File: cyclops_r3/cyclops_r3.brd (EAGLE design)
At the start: 124.5 x 79.9 mm, 96 parts, among them Q1 BC817, Q2 IRF510, U1 MCP4921, U2 317-N, U3 TLV3701, U4 337-N, U5 ADR03, U6 OP1177, U7 LTC2052, U8 ZXTD45

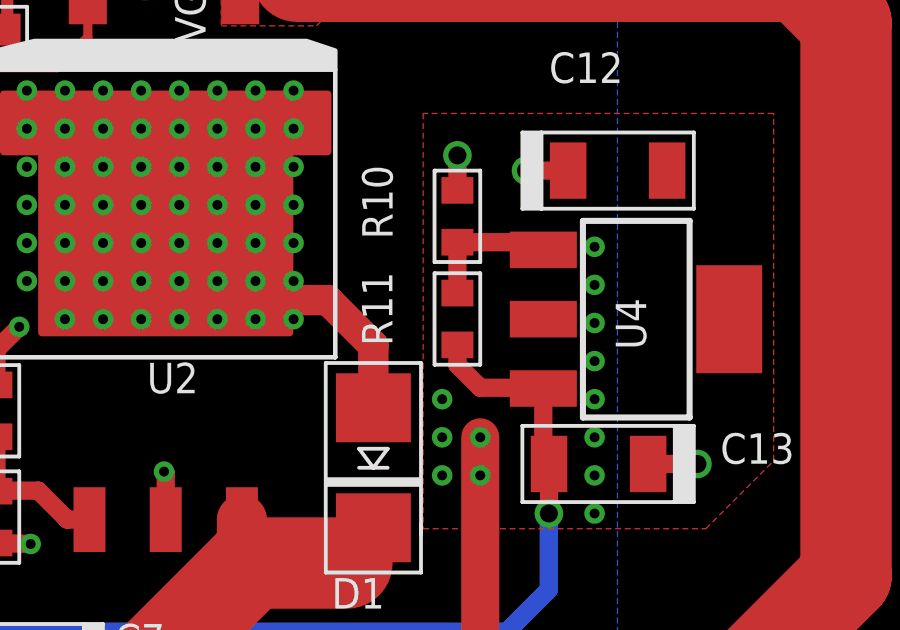
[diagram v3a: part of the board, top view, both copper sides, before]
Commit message: Added some components for the photodiode. Fixed up power supply rails for driver.
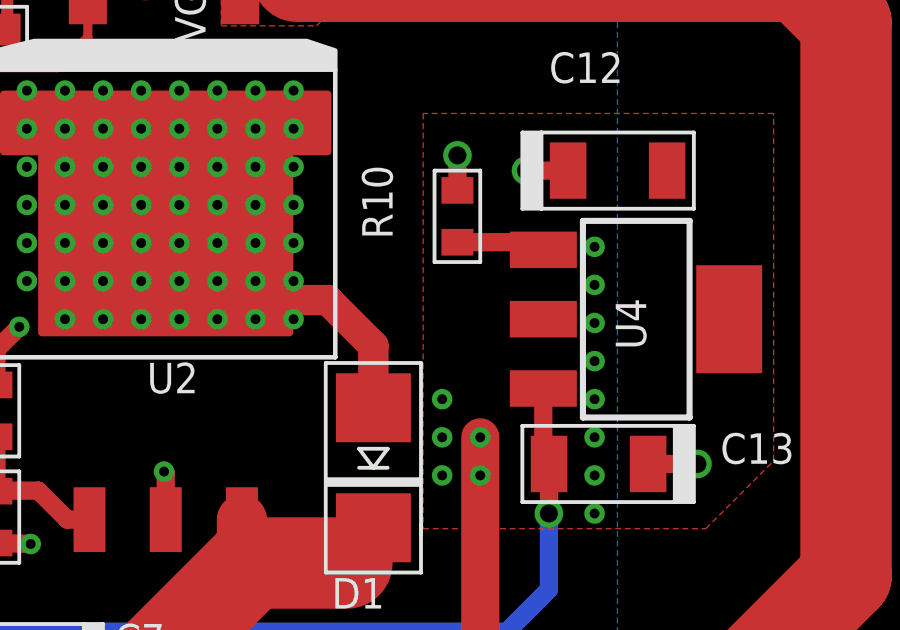
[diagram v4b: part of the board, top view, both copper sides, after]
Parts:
- removed R11: 120, cyclops:0603
- R10: value 75 -> 0
- R6: value 2.1k -> 1.82k
- U7: value LTC2052 -> LTC2052HV
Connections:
- removed net -2.1V: C13.-, C21.1, C23.1, R11.1, R16.1, U4.3, U7.11
- new net -1.25V: C13.-, C21.1, C23.1, R16.1, U4.3, U7.11
- net N$12: no longer R11.2
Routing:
- net -2.1V: track 74.3 -> 0.00 mm, vias 2 -> 0
- net -1.25V: track 0.00 -> 70.4 mm, vias 0 -> 2
- net N$12: track 4.66 -> 2.97 mm
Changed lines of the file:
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@@
 </autorouter>
 <elements>
-<element name="U7" library="cyclops" package="SO14" value="LTC2052" x="67.684" y="43.18" smashed="yes" rot="R270">
+<element name="U7" library="cyclops" package="SO14" value="LTC2052HV" x="67.684" y="43.18" smashed="yes" rot="R270">
 <attribute name="NAME" x="69.088" y="48.013" size="1.016" layer="25" font="vector" ratio="18"/>
-<attribute name="VALUE" x="68.065" y="40.259" size="1.016" layer="27" font="vector" ratio="18" rot="R90"/>
+<attribute name="VALUE" x="67.557" y="38.989" size="1.016" layer="27" font="vector" ratio="18" rot="R90"/>
 </element>
 <element name="REF_ADJ" library="cyclops" package="SM-42/43W" value="10k" x="65.525" y="24.511" smashed="yes" rot="R180">
@@
 <attribute name="VALUE" x="99.187" y="22.105" size="1.016" layer="27" font="vector" ratio="18"/>
 </element>
-<element name="R6" library="cyclops" package="0603" value="2.1k" x="88.011" y="26.296" smashed="yes" rot="R90">
+<element name="R6" library="cyclops" package="0603" value="1.82k" x="88.011" y="26.296" smashed="yes" rot="R90">
 <attribute name="MN" value="Panasonic" x="88.011" y="26.296" size="1.778" layer="27" rot="R90" display="off"/>
 <attribute name="DK" value="PxxxxHTR-ND" x="88.011" y="26.296" size="1.778" layer="27" rot="R90" display="off"/>
@@
 <attribute name="VALUE" x="112.141" y="26.931" size="1.016" layer="27" font="vector" ratio="18"/>
 </element>
-<element name="R11" library="cyclops" package="0603" value="120" x="103.378" y="32.9" smashed="yes" rot="R90">
-<attribute name="MN" value="Panasonic" x="103.378" y="32.9" size="0.889" layer="27" font="vector" ratio="18" rot="R90" display="off"/>
-<attribute name="DK" value="PxxxxHTR-ND" x="103.378" y="32.9" size="0.889" layer="27" font="vector" ratio="18" rot="R90" display="off"/>
-<attribute name="MPN" value="ERJ-3EKFxxxxV" x="103.378" y="32.9" size="0.889" layer="27" font="vector" ratio="18" rot="R90" display="off"/>
-<attribute name="NAME" x="100.704" y="32.004" size="1.016" layer="25" font="vector" ratio="18" rot="R270" align="center-right"/>
-<attribute name="VALUE" x="101.847" y="32.004" size="1.016" layer="27" font="vector" ratio="18" rot="R90" align="center-left"/>
-</element>
-<element name="R10" library="cyclops" package="0603" value="75" x="103.378" y="36.322" smashed="yes" rot="R90">
+<element name="R10" library="cyclops" package="0603" value="0" x="103.378" y="36.322" smashed="yes" rot="R90">
 <attribute name="MN" value="Panasonic" x="103.378" y="36.322" size="0.889" layer="27" font="vector" ratio="18" rot="R90" display="off"/>
 <attribute name="DK" value="PxxxxHTR-ND" x="103.378" y="36.322" size="0.889" layer="27" font="vector" ratio="18" rot="R90" display="off"/>
@@
 </signal>
 <signal name="N$12">
-<contactref element="R11" pad="2"/>
 <contactref element="R10" pad="1"/>
 <contactref element="U4" pad="1"/>
-<wire x1="103.378" y1="33.7636" x2="103.378" y2="35.4584" width="0.6096" layer="1"/>
 <wire x1="103.378" y1="35.4584" x2="105.9872" y2="35.4584" width="0.6096" layer="1"/>
 <wire x1="105.9872" y1="35.4584" x2="106.2412" y2="35.2044" width="0.6096" layer="1"/>
 </signal>
-<signal name="-2.1V">
-<contactref element="R11" pad="1"/>
+<signal name="-1.25V">
 <contactref element="U4" pad="3"/>
 <contactref element="C13" pad="-"/>
@@
 <wire x1="106.433" y1="28.067" x2="106.2412" y2="28.067" width="0.6096" layer="1"/>
 <wire x1="106.2412" y1="28.067" x2="106.2412" y2="30.5816" width="0.6096" layer="1"/>
-<wire x1="103.378" y1="32.0364" x2="103.378" y2="31.369" width="0.6096" layer="1"/>
-<wire x1="103.378" y1="31.369" x2="104.14" y2="30.607" width="0.6096" layer="1"/>
-<wire x1="104.14" y1="30.607" x2="106.2666" y2="30.607" width="0.6096" layer="1"/>
 <wire x1="106.934" y1="30.607" x2="106.2666" y2="30.607" width="0.6096" layer="1"/>
 <wire x1="106.2666" y1="30.607" x2="106.2412" y2="30.5816" width="0.6096" layer="1"/>

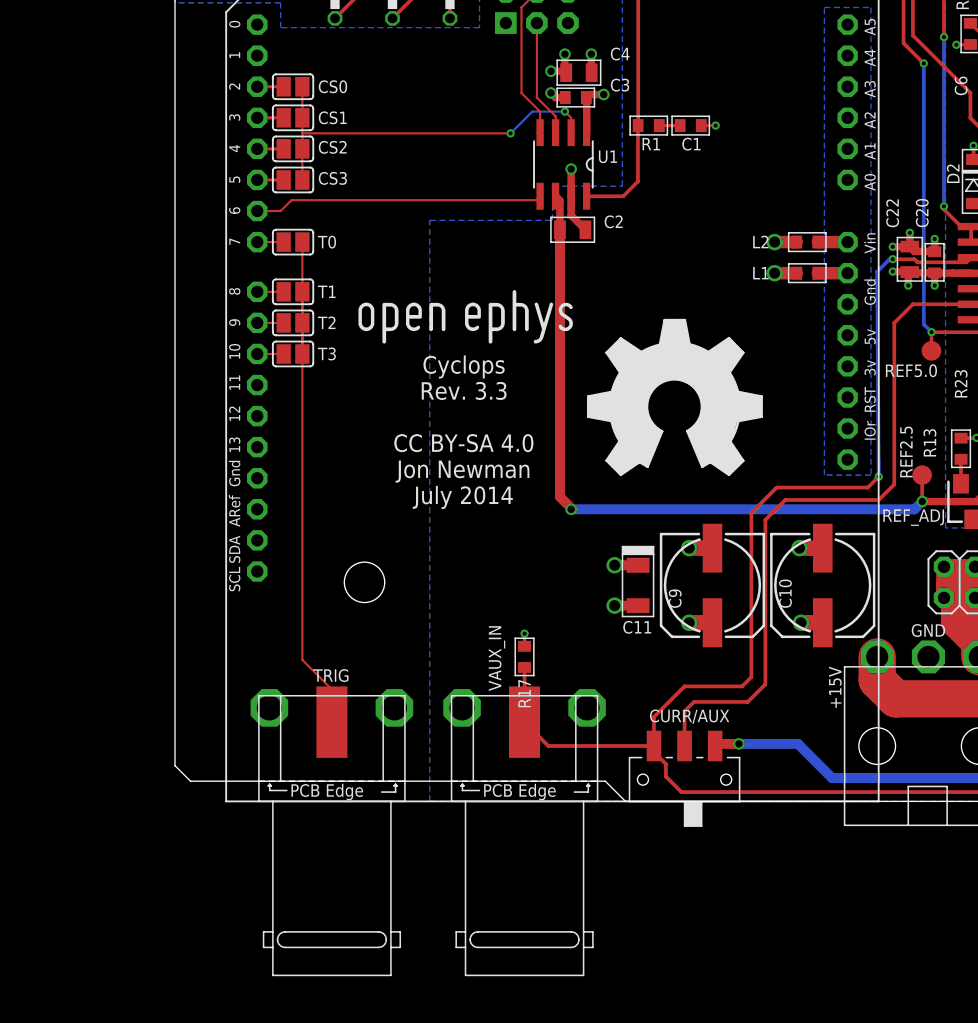
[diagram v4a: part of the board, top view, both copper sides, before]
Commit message: Added digital overcurrent protection.
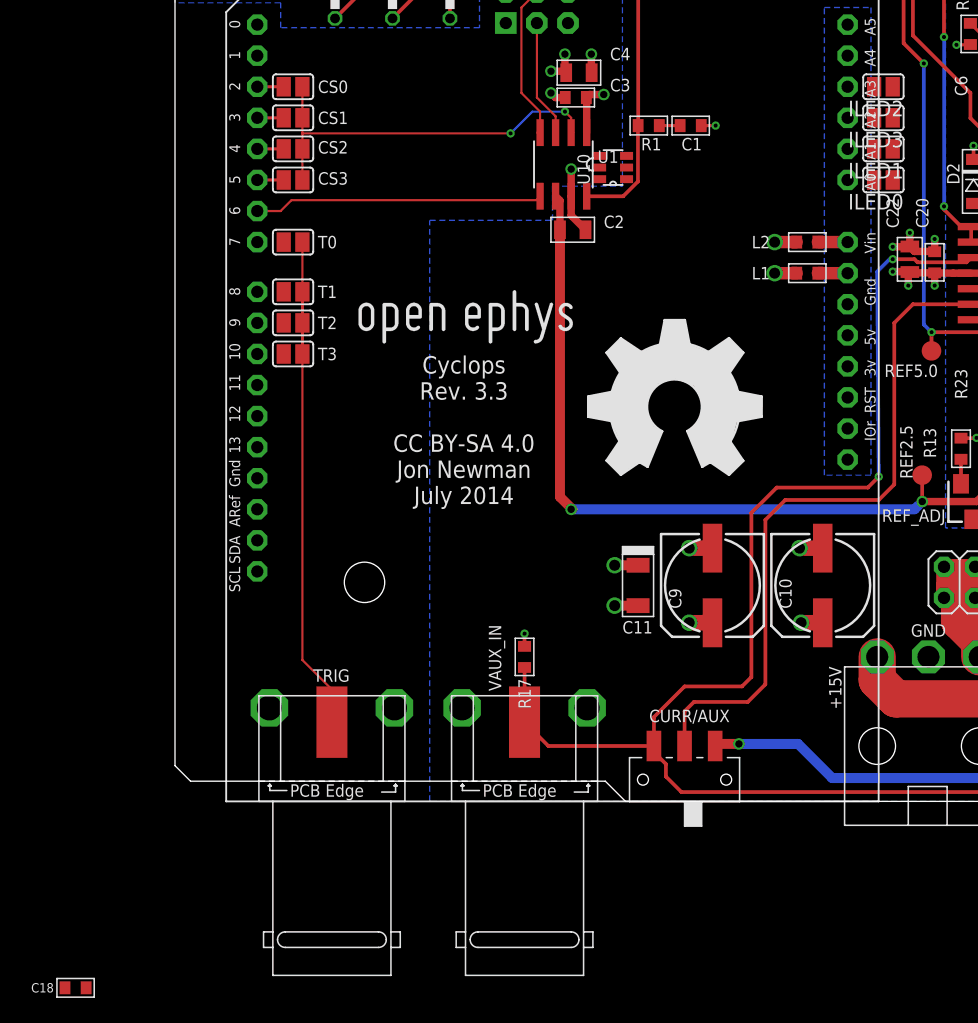
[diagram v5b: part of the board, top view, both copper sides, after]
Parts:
- added C18: .1uF, cyclops:0603
- added ILED0, ILED1, ILED2, ILED3: (no value), cyclops:SJ
- added U10: MCP4022, cyclops:SOT23-6
- R22: value 5.6k -> 5.6k DNP
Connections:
- net +12V renamed +11V
- net VCTL_PRE renamed N$34
- new net N$19: LEONARDO.A1
- new net N$21: LEONARDO.A2
- new net N$23: LEONARDO.A3
- new net N$24: C18.2, U10.2
- new net N$7: LEONARDO.A0
- new net POT: LEONARDO.D7, U10.3
- new net VCTL_PROTECT: GAIN.3, R22.1, U10.5
- net CS: now also U10.4
- net N$16: now also C18.1, U10.1; no longer GAIN.3, R22.1
- net REF2.5: now also LEONARDO.AREF
- net T0: now also LEONARDO.D8; no longer LEONARDO.D7
- net T1: now also LEONARDO.D9; no longer LEONARDO.D8
- net T2: now also LEONARDO.D10; no longer LEONARDO.D9
- net T3: now also LEONARDO.D11; no longer LEONARDO.D10
- net VCTL: now also U10.6
- net VI: now also ILED0.1, ILED1.1, ILED2.1, ILED3.1
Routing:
- net VCTL_PROTECT: track 0.00 -> 2.61 mm
- net N$16: track 2.61 -> 0.00 mm
- net T3: track 2.17 -> 0.00 mm
- net T2: track 2.17 -> 0.00 mm
- net T1: track 2.17 -> 0.00 mm
- net T0: track 2.17 -> 0.00 mm
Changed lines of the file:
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@@
 <attribute name="VALUE" x="25.019" y="2.032" size="1.016" layer="27" font="vector" ratio="18"/>
 </element>
-<element name="R22" library="cyclops" package="0603" value="5.6k" x="33.02" y="72.898" smashed="yes">
+<element name="R22" library="cyclops" package="0603" value="5.6k DNP" x="33.02" y="72.898" smashed="yes">
 <attribute name="MN" value="Panasonic" x="33.02" y="72.898" size="1.778" layer="27" display="off"/>
 <attribute name="DK" value="PxxxxHTR-ND" x="33.02" y="72.898" size="1.778" layer="27" display="off"/>
@@
 <attribute name="VALUE" x="20.32" y="0.508" size="1.016" layer="27" font="vector" ratio="18" rot="R90"/>
 </element>
+<element name="ILED0" library="cyclops" package="SJ" value="" x="57.912" y="50.8" rot="R180"/>
+<element name="ILED1" library="cyclops" package="SJ" value="" x="57.912" y="53.34" rot="R180"/>
+<element name="ILED2" library="cyclops" package="SJ" value="" x="57.912" y="58.42" rot="R180"/>
+<element name="ILED3" library="cyclops" package="SJ" value="" x="57.912" y="55.88" rot="R180"/>
+<element name="U10" library="cyclops" package="SOT23-6" value="MCP4022" x="35.814" y="51.816" rot="R90"/>
+<element name="C18" library="cyclops" package="0603" value=".1uF" x="-8.128" y="-15.24"/>
 </elements>
 <signals>
@@
 <via x="27.432" y="54.61" extent="1-16" drill="0.3302"/>
 <wire x1="27.432" y1="54.61" x2="10.414" y2="54.61" width="0.1778" layer="1"/>
+<contactref element="U10" pad="4"/>
+<wire x1="34.714" y1="52.766" x2="10.414" y2="50.8" width="0" layer="19" extent="1-1"/>
 </signal>
 <signal name="DACA">
@@
 <wire x1="61.08" y1="26.67" x2="61.08" y2="24.518" width="0.3048" layer="1"/>
 <wire x1="61.08" y1="24.518" x2="61.087" y2="24.511" width="0.3048" layer="1"/>
+<contactref element="LEONARDO" pad="AREF"/>
+<wire x1="6.724" y1="23.876" x2="31.4706" y2="24.892" width="0" layer="19" extent="1-1"/>
 </signal>
 <signal name="VAUX">
@@
 <wire x1="70.284" y1="39.37" x2="70.919" y2="38.735" width="0.3048" layer="1"/>
 <wire x1="70.919" y1="38.735" x2="73.8054" y2="38.735" width="0.3048" layer="1"/>
+<contactref element="ILED0" pad="1"/>
+<contactref element="ILED1" pad="1"/>
+<contactref element="ILED2" pad="1"/>
+<contactref element="ILED3" pad="1"/>
+<wire x1="58.674" y1="55.88" x2="58.674" y2="58.42" width="0" layer="19" extent="1-1"/>
+<wire x1="58.674" y1="53.34" x2="58.674" y2="55.88" width="0" layer="19" extent="1-1"/>
+<wire x1="58.674" y1="50.8" x2="58.674" y2="53.34" width="0" layer="19" extent="1-1"/>
+<wire x1="68.453" y1="61.3718125" x2="58.674" y2="58.42" width="0" layer="19" extent="1-1"/>
 </signal>
 <signal name="_VREF">
@@
 <wire x1="49.276" y1="74.168" x2="50.167" y2="73.277" width="0.3048" layer="1"/>
 <wire x1="50.167" y1="73.277" x2="50.167" y2="72.731" width="0.3048" layer="1"/>
+<contactref element="U10" pad="6"/>
+<wire x1="34.714" y1="50.866" x2="33.8836" y2="72.898" width="0" layer="19" extent="1-1"/>
 </signal>
 <signal name="N$6">
@@
 <wire x1="39.5916" y1="55.245" x2="41.2934" y2="55.245" width="0.254" layer="1"/>
 </signal>
-<signal name="VCTL_PRE">
+<signal name="N$34">
 <contactref element="S2" pad="3"/>
 <contactref element="DAC/VCTL" pad="2"/>
@@
 <wire x1="54.984" y1="45.72" x2="52.5526" y2="45.72" width="1.016" layer="1"/>
 </signal>
-<signal name="+12V" class="1">
+<signal name="+11V" class="1">
 <via x="51.181" y="14.605" extent="1-16" drill="0.9"/>
 <via x="42.037" y="14.605" extent="1-16" drill="0.9"/>
@@
 <via x="62.865" y="62.484" extent="1-16" drill="0.3302"/>
 </signal>
-<signal name="N$16">
+<signal name="VCTL_PROTECT">
 <contactref element="GAIN" pad="3"/>
 <contactref element="R22" pad="1"/>
 <wire x1="31.369" y1="75.184" x2="31.369" y2="73.6854" width="0.3048" layer="1"/>
 <wire x1="31.369" y1="73.6854" x2="32.1564" y2="72.898" width="0.3048" layer="1"/>
+<contactref element="U10" pad="5"/>
+<wire x1="34.714" y1="51.816" x2="32.1564" y2="72.898" width="0" layer="19" extent="1-1"/>
 </signal>
 <signal name="LED-">
@@
 <signal name="T0">
 <contactref element="T0" pad="2"/>
-<contactref element="LEONARDO" pad="D7"/>
-<wire x1="8.89" y1="45.72" x2="6.724" y2="45.72" width="0.1778" layer="1"/>
+<contactref element="LEONARDO" pad="D8"/>
+<wire x1="6.724" y1="41.656" x2="8.89" y2="45.72" width="0" layer="19" extent="1-1"/>
 </signal>
 <signal name="T1">
 <contactref element="T1" pad="2"/>
-<contactref element="LEONARDO" pad="D8"/>
-<wire x1="8.89" y1="41.656" x2="6.724" y2="41.656" width="0.1778" layer="1"/>
+<contactref element="LEONARDO" pad="D9"/>
+<wire x1="6.724" y1="39.116" x2="8.89" y2="41.656" width="0" layer="19" extent="1-1"/>
 </signal>
 <signal name="T2">
 <contactref element="T2" pad="2"/>
-<contactref element="LEONARDO" pad="D9"/>
-<wire x1="8.89" y1="39.116" x2="6.724" y2="39.116" width="0.1778" layer="1"/>
+<contactref element="LEONARDO" pad="D10"/>
+<wire x1="6.724" y1="36.576" x2="8.89" y2="39.116" width="0" layer="19" extent="1-1"/>
 </signal>
 <signal name="T3">
 <contactref element="T3" pad="2"/>
-<contactref element="LEONARDO" pad="D10"/>
-<wire x1="8.89" y1="36.576" x2="6.724" y2="36.576" width="0.1778" layer="1"/>
+<contactref element="LEONARDO" pad="D11"/>
+<wire x1="6.724" y1="34.036" x2="8.89" y2="36.576" width="0" layer="19" extent="1-1"/>
+</signal>
+<signal name="N$7">
+<contactref element="LEONARDO" pad="A0"/>
+</signal>
+<signal name="N$19">
+<contactref element="LEONARDO" pad="A1"/>
+</signal>
+<signal name="N$21">
+<contactref element="LEONARDO" pad="A2"/>
+</signal>
+<signal name="N$23">
+<contactref element="LEONARDO" pad="A3"/>
+</signal>
+<signal name="N$16">
+<contactref element="U10" pad="1"/>
+<contactref element="C18" pad="1"/>
+<wire x1="-8.9916" y1="-15.24" x2="36.914" y2="50.866" width="0" layer="19" extent="1-1"/>
+</signal>
+<signal name="N$24">
+<contactref element="U10" pad="2"/>
+<contactref element="C18" pad="2"/>
+<wire x1="-7.2644" y1="-15.24" x2="36.914" y2="51.816" width="0" layer="19" extent="1-1"/>
+</signal>
+<signal name="POT">
+<contactref element="U10" pad="3"/>
+<contactref element="LEONARDO" pad="D7"/>
+<wire x1="36.914" y1="52.766" x2="6.724" y2="45.72" width="0" layer="19" extent="1-1"/>
 </signal>
 </signals>
